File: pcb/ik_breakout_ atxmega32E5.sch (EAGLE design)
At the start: 31 parts, among them IC1 FT230XS, J1 AVR_SPI_PRG_62X3_LOCK, U1 MIC5219 3.3V

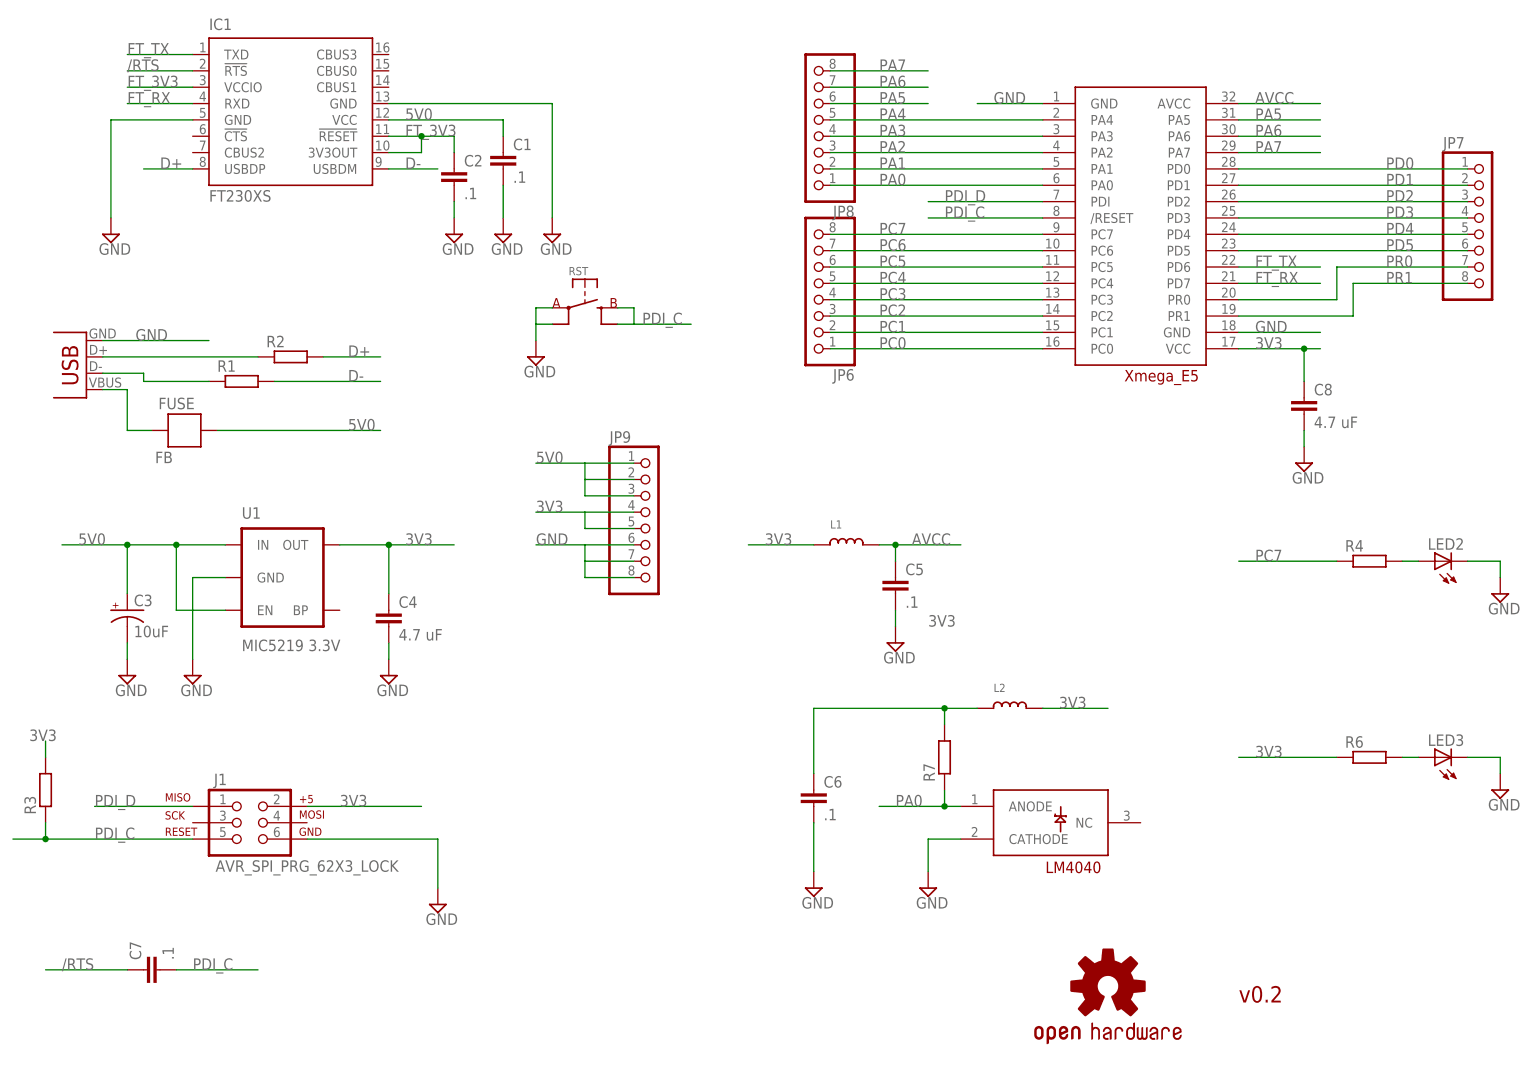
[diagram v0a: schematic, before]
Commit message: oops. committed from /pcb/fab/gerbers folder.
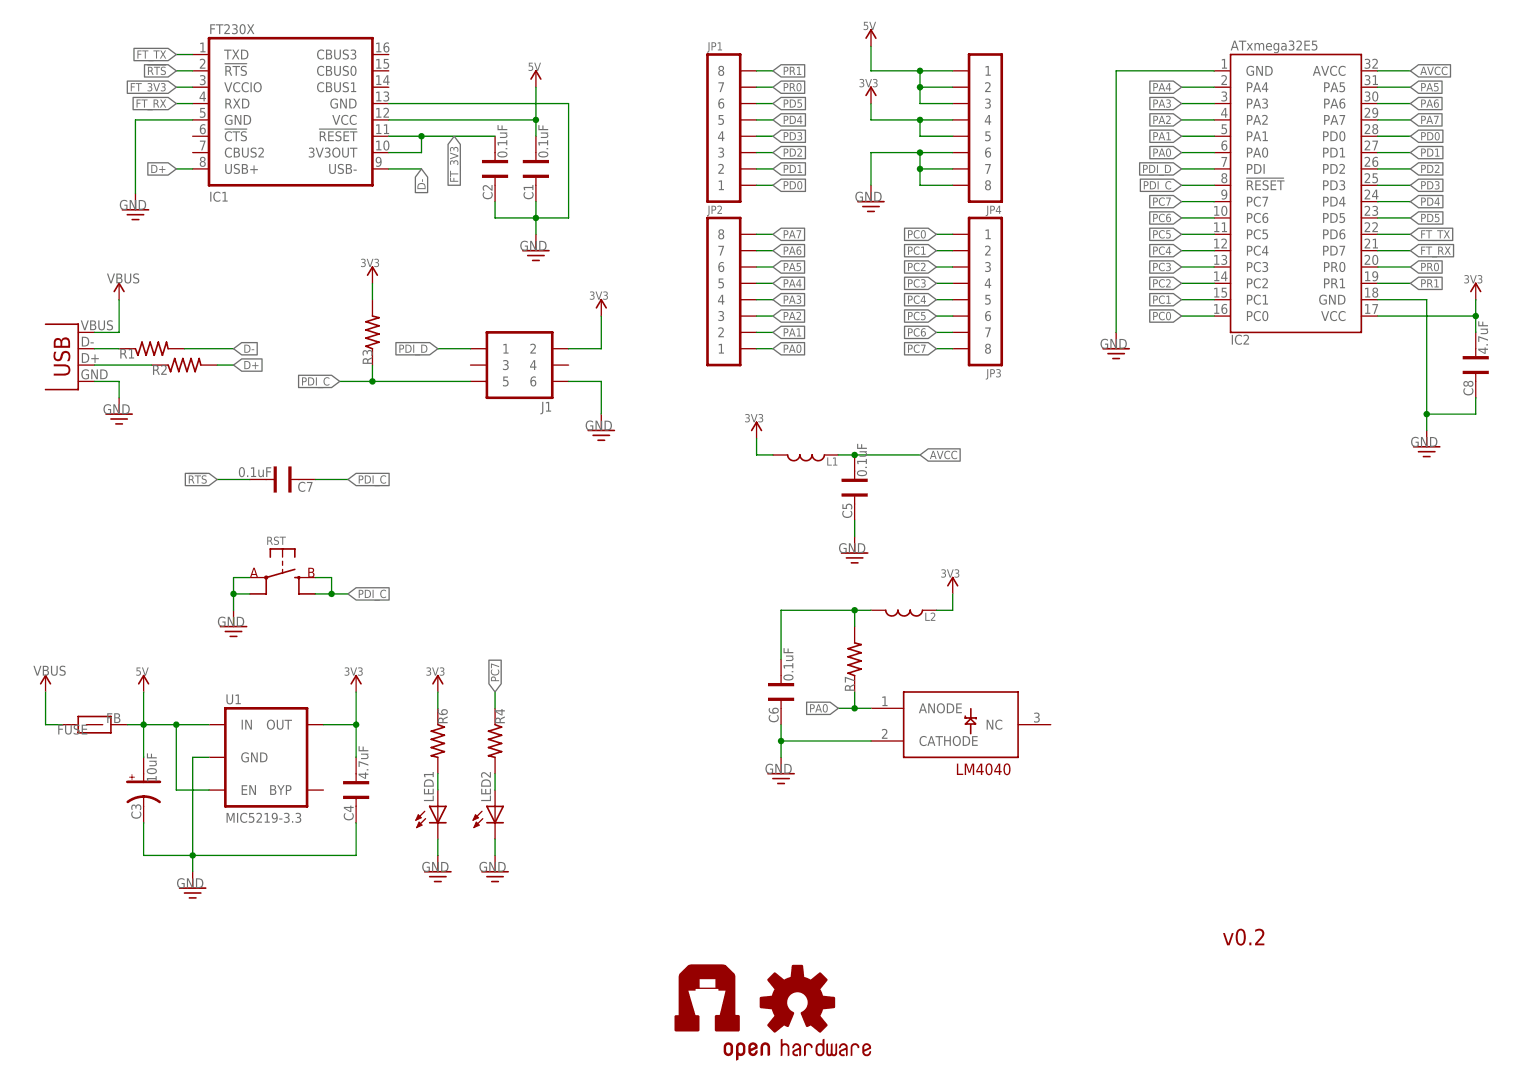
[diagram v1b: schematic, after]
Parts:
- removed JP6, JP7, JP8, JP9: (no value), microbuilder:HEADER-1X8ROUND
- removed LED3: (no value), SparkFun-LED:LED0603
- removed U$1: IHSAN_XMEGA_E5, SparkFun-DigitalIC_ihsan:IHSAN_XMEGA_E5
- removed U$2: IHSAN_LM4040, SparkFun-DigitalIC_ihsan:IHSAN_LM4040
- added IC2: ATXMEGA32E5, Ai_IC:ATXMEGA32E5
- added JP1, JP2, JP3, JP4: 1X08NOFIRST, Ai_Connectors:1X08NOFIRST
- added LED1: (no value), Ai_LED:LED0603
- added U$3: AI-LOGOXS, Ai_Miscellany:AI-LOGOXS
- added U2: IHSAN_LM4040, SparkFun-DigitalIC_ihsan:IHSAN_LM4040
- C1, C2, C5, C6, C7: value .1 -> 0.1uF; device rcl:C-EUC0603 -> Ai_Passives:CAP0603
- C3: device SparkFun-Capacitors:10UF-TANT -> Ai_Passives:CAP-POLEIA3216
- C4, C8: value 4.7 uF -> 4.7uF; device rcl:C-EUC0603 -> Ai_Passives:CAP0603
- FUSE: device SparkFun-Passives:FB -> Ai_Passives:FB
- IC1: value FT230XS -> FT230X; device ftdichip:FT230XS -> Ai_IC:FT230X
- J1: value AVR_SPI_PRG_62X3_LOCK -> 2X03; device SparkFun-Connectors:AVR_SPI_PRG_62X3_LOCK -> Ai_Connectors:2X03
- L1, L2: device microbuilder:INDUCTOR0603 -> Ai_Passives:IND0603
- LED2: device SparkFun-LED:LED0603 -> Ai_LED:LED0603
- R1, R2, R3, R4, R6, R7: device rcl:R-EU_R0603 -> Ai_Passives:RES0603
- U1: value MIC5219 3.3V -> MIC5219-3.3; device SparkFun-PowerIC:V_REG_MIC52193.3V -> Ai_Power:MIC5219-3.3
- USB1: value USBMICROB-SMD -> USBMICROB-TH; device Ai_Connectors:USBMICROB-SMD -> Ai_Connectors:USBMICROB-TH
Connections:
- net /RTS renamed !RTS
- removed net 5V0: C1.1, C3.+, FUSE.P$1, IC1.VCC, JP9.1, JP9.2, JP9.3, U1.EN, U1.IN
- removed net N$10: FUSE.P$2, USB1.VBUS
- new net 5V: C1.1, C3.A, FUSE.P$2, IC1.VCC, JP4.1, JP4.2, JP4.3, U1.EN, U1.IN
- new net VBUS: FUSE.P$1, USB1.VBUS
- net 3V3: now also IC2.VCC, JP4.4, JP4.5; no longer JP9.4, JP9.5, U$1.VCC
- net AVCC: now also IC2.AVCC; no longer U$1.AVCC
- net D+: now also IC1.USB+; no longer IC1.USBDP
- net D-: now also IC1.USB-; no longer IC1.USBDM
- net FT_RX: now also IC2.PD7; no longer U$1.PD7
- net FT_TX: now also IC2.PD6; no longer U$1.PD6
- net GND: now also C3.C, IC1.GND@2, IC2.GND@1, IC2.GND@2, JP4.6, JP4.7, JP4.8, LED1.C, U2.CATHODE; no longer C3.-, IC1.GND, JP9.6, JP9.7, JP9.8, LED3.C, U$1.GND@1, U$1.GND@2, U$2.CATHODE
- net N$8: now also LED1.A; no longer LED3.A
- net PA0: now also IC2.PA0, JP2.1, U2.ANODE; no longer JP8.1, U$1.PA0, U$2.ANODE
- net PA1: now also IC2.PA1, JP2.2; no longer JP8.2, U$1.PA1
- net PA2: now also IC2.PA2, JP2.3; no longer JP8.3, U$1.PA2
- net PA3: now also IC2.PA3, JP2.4; no longer JP8.4, U$1.PA3
- net PA4: now also IC2.PA4, JP2.5; no longer JP8.5, U$1.PA4
- net PA5: now also IC2.PA5, JP2.6; no longer JP8.6, U$1.PA5
- net PA6: now also IC2.PA6, JP2.7; no longer JP8.7, U$1.PA6
- net PA7: now also IC2.PA7, JP2.8; no longer JP8.8, U$1.PA7
- net PC0: now also IC2.PC0, JP3.1; no longer JP6.1, U$1.PC0
- net PC1: now also IC2.PC1, JP3.2; no longer JP6.2, U$1.PC1
- net PC2: now also IC2.PC2, JP3.3; no longer JP6.3, U$1.PC2
- net PC3: now also IC2.PC3, JP3.4; no longer JP6.4, U$1.PC3
- net PC4: now also IC2.PC4, JP3.5; no longer JP6.5, U$1.PC4
- net PC5: now also IC2.PC5, JP3.6; no longer JP6.6, U$1.PC5
- net PC6: now also IC2.PC6, JP3.7; no longer JP6.7, U$1.PC6
- net PC7: now also IC2.PC7, JP3.8; no longer JP6.8, U$1.PC7
- net PD0: now also IC2.PD0, JP1.1; no longer JP7.1, U$1.PD0
- net PD1: now also IC2.PD1, JP1.2; no longer JP7.2, U$1.PD1
- net PD2: now also IC2.PD2, JP1.3; no longer JP7.3, U$1.PD2
- net PD3: now also IC2.PD3, JP1.4; no longer JP7.4, U$1.PD3
- net PD4: now also IC2.PD4, JP1.5; no longer JP7.5, U$1.PD4
- net PD5: now also IC2.PD5, JP1.6; no longer JP7.6, U$1.PD5
- net PDI_C: now also IC2.!RESET; no longer U$1./RESET
- net PDI_D: now also IC2.PDI; no longer U$1.PDI
- net PR0: now also IC2.PR0, JP1.7; no longer JP7.7, U$1.PR0
- net PR1: now also IC2.PR1, JP1.8; no longer JP7.8, U$1.PR1
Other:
- moved on the sheet: C1, C2, C4, C5, C6, C7, C8, LED2, RST, U1

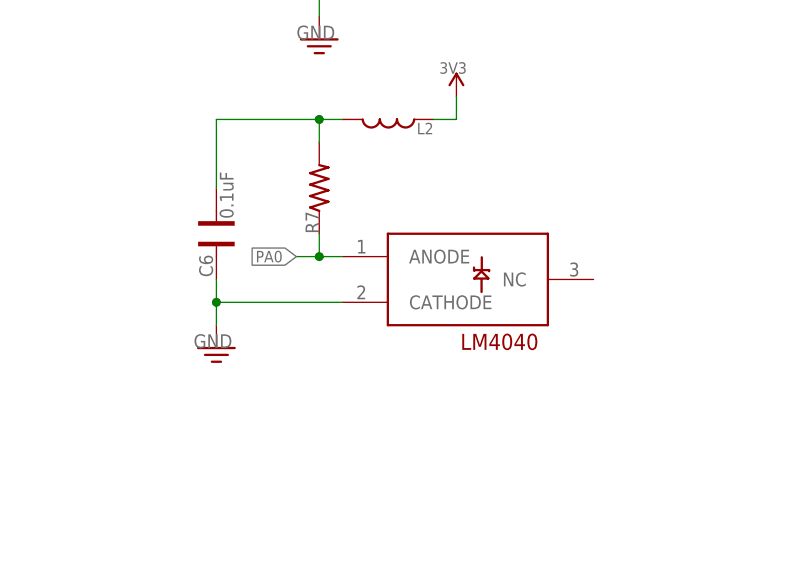
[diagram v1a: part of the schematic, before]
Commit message: changed LM4040 to include part on Ai_Power library
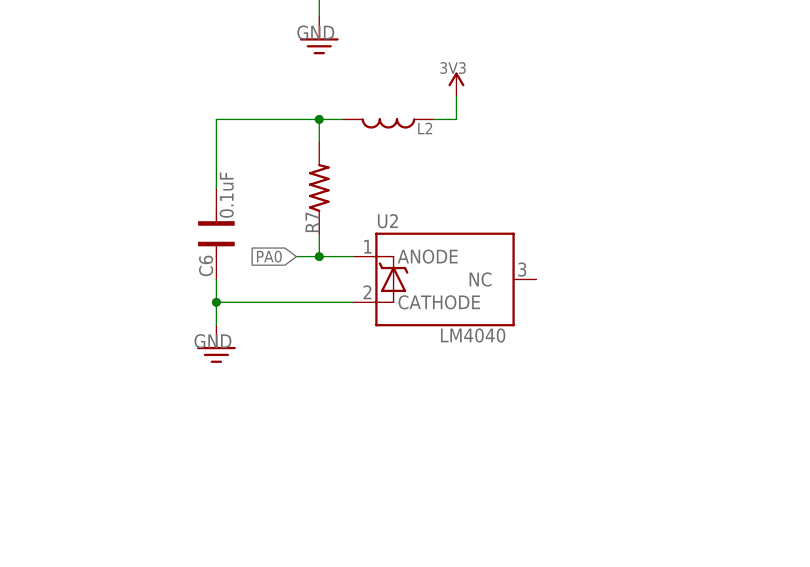
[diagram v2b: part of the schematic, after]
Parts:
- U2: value IHSAN_LM4040 -> LM4040; device SparkFun-DigitalIC_ihsan:IHSAN_LM4040 -> Ai_Power:LM4040
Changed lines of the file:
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@@
 <part name="C6" library="Ai_Passives" deviceset="CAP" device="0603" value="0.1uF"/>
 <part name="SUPPLY11" library="Ai_Power" deviceset="GND" device=""/>
-<part name="U2" library="SparkFun-DigitalIC_ihsan" deviceset="IHSAN_LM4040" device=""/>
+<part name="U2" library="Ai_Power" deviceset="LM4040" device=""/>
 <part name="FUSE" library="Ai_Passives" deviceset="FB" device=""/>
 <part name="USB1" library="Ai_Connectors" deviceset="USB" device="MICROB-TH" value="USBMICROB-TH"/>
@@
 <instance part="C6" gate="G$1" x="129.54" y="60.96"/>
 <instance part="SUPPLY11" gate="GND" x="129.54" y="48.26"/>
-<instance part="U2" gate="G$1" x="153.67" y="53.34"/>
+<instance part="U2" gate="G$1" x="154.94" y="55.88"/>
 <instance part="FUSE" gate="G$1" x="22.86" y="55.88" rot="MR180"/>
 <instance part="USB1" gate="G$1" x="16.51" y="113.03" rot="MR0"/>
@@
 <wire x1="129.54" y1="53.34" x2="129.54" y2="55.88" width="0.1524" layer="91"/>
 <pinref part="U2" gate="G$1" pin="CATHODE"/>
-<wire x1="143.51" y1="53.34" x2="129.54" y2="53.34" width="0.1524" layer="91"/>
+<wire x1="144.78" y1="53.34" x2="129.54" y2="53.34" width="0.1524" layer="91"/>
 <junction x="129.54" y="53.34"/>
 </segment>
@@
 <wire x1="138.43" y1="58.42" x2="140.97" y2="58.42" width="0.1524" layer="91"/>
 <pinref part="R7" gate="G$1" pin="1"/>
-<wire x1="140.97" y1="58.42" x2="143.51" y2="58.42" width="0.1524" layer="91"/>
+<wire x1="140.97" y1="58.42" x2="144.78" y2="58.42" width="0.1524" layer="91"/>
 <wire x1="140.97" y1="60.96" x2="140.97" y2="58.42" width="0.1524" layer="91"/>
 <junction x="140.97" y="58.42"/>
